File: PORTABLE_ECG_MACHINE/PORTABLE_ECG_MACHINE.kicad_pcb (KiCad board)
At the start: 2 copper layers, 25.5 x 64.8 mm, 71 parts, among them IC1 AD8232ACPZ, J1 UART, J2 Li-Ion 3.7 CONN, J3 USB_B_Micro, Q1 BSS138, Q2 BSS138, SW1 SW_SPDT, U1 SSD1306, U2 CP2102-GM, U3 TC1262-33, U4 TP4056

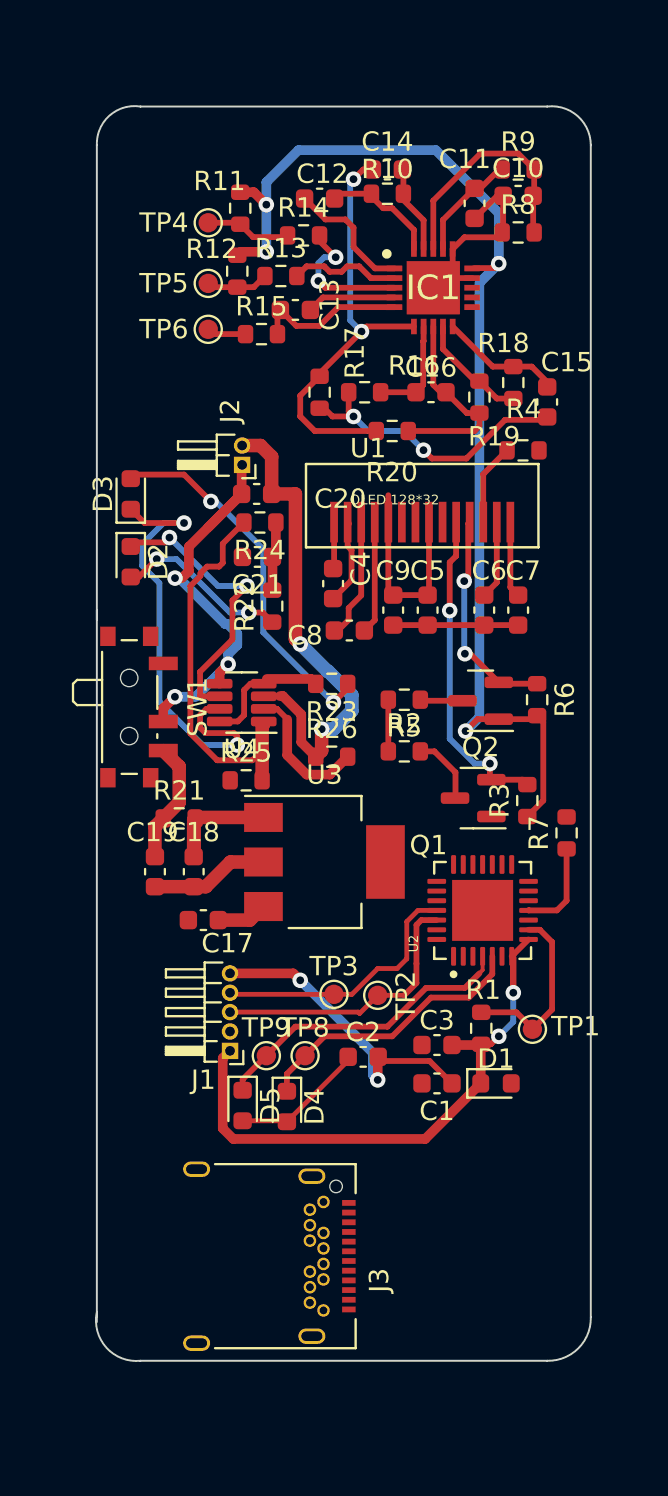
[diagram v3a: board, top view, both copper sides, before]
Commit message: Fill Zone add | Edgecut complete
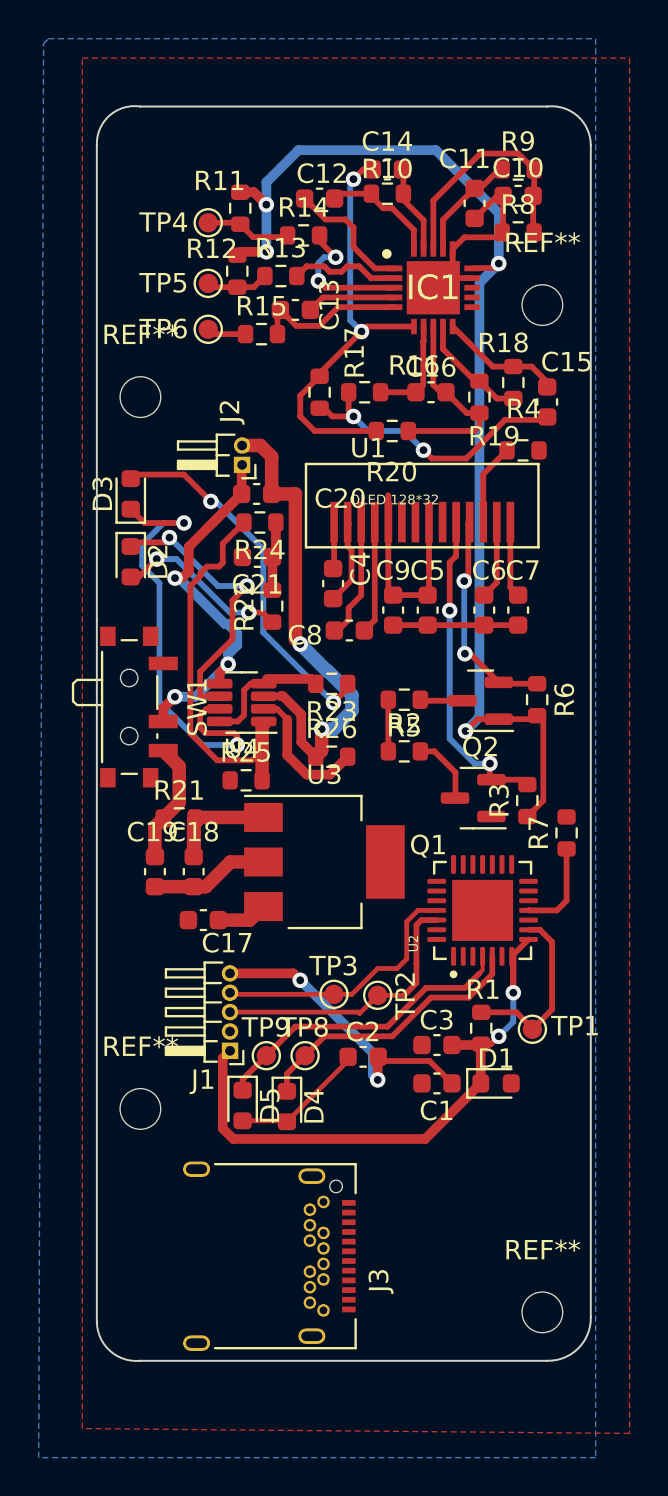
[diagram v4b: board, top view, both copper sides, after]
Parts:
- added REF**: MountingHole_2.1mm, MountingHole:MountingHole_2.1mm, F.Cu at (107.0, 34.8)
- added REF**: MountingHole_2.1mm, MountingHole:MountingHole_2.1mm, F.Cu at (86.2, 76.2)
- added REF**: MountingHole_2.1mm, MountingHole:MountingHole_2.1mm, F.Cu at (86.2, 39.5)
- added REF**: MountingHole_2.1mm, MountingHole:MountingHole_2.1mm, F.Cu at (107.0, 86.8)
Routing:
- added copper zone on B.Cu, net GND
- added copper zone on F.Cu, net GND
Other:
- outline, holes or cut-outs redrawn
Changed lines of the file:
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@@
     )
   )
+  (footprint "MountingHole:MountingHole_2.1mm" (layer "F.Cu")
+    (at 107 34.75)
+    (descr "Mounting Hole 2.1mm, no annular")
+    (tags "mounting hole 2.1mm no annular")
+    (attr exclude_from_pos_files exclude_from_bom)
+    (fp_text reference "REF**" (at 0 -3.2) (layer "F.SilkS")
+      (effects (font (size 1 1) (thickness 0.15)))
+    )
+    (fp_text value "MountingHole_2.1mm" (at 0 3.2) (layer "F.Fab")
+      (effects (font (size 1 1) (thickness 0.15)))
+    )
+    (fp_text user "${REFERENCE}" (at 0 0) (layer "F.Fab")
+      (effects (font (size 1 1) (thickness 0.15)))
+    )
+    (fp_circle (center 0 0) (end 2.1 0) (layer "Cmts.User") (width 0.15) (fill none))
+    (fp_circle (center 0 0) (end 2.35 0) (layer "F.CrtYd") (width 0.05) (fill none))
+    (pad "" np_thru_hole circle (at 0 0) (size 2.1 2.1) (drill 2.1) (layers *.Cu *.Mask))
+  )
   (footprint "Resistor_SMD:R_0603_1608Metric" (layer "F.Cu")
     (at 93.5 33.25)
@@
       (net 25 "/RA") (pinfunction "1") (pintype "passive"))
   )
+  (footprint "MountingHole:MountingHole_2.1mm" (layer "F.Cu")
+    (at 86.25 76.25)
+    (descr "Mounting Hole 2.1mm, no annular")
+    (tags "mounting hole 2.1mm no annular")
+    (attr exclude_from_pos_files exclude_from_bom)
+    (fp_text reference "REF**" (at 0 -3.2) (layer "F.SilkS")
+      (effects (font (size 1 1) (thickness 0.15)))
+    )
+    (fp_text value "MountingHole_2.1mm" (at 0 3.2) (layer "F.Fab")
+      (effects (font (size 1 1) (thickness 0.15)))
+    )
+    (fp_text user "${REFERENCE}" (at 0 0) (layer "F.Fab")
+      (effects (font (size 1 1) (thickness 0.15)))
+    )
+    (fp_circle (center 0 0) (end 2.1 0) (layer "Cmts.User") (width 0.15) (fill none))
+    (fp_circle (center 0 0) (end 2.35 0) (layer "F.CrtYd") (width 0.05) (fill none))
+    (pad "" np_thru_hole circle (at 0 0) (size 2.1 2.1) (drill 2.1) (layers *.Cu *.Mask))
+  )
   (footprint "Capacitor_SMD:C_0603_1608Metric" (layer "F.Cu")
     (at 99 27.75)
@@
     )
   )
+  (footprint "MountingHole:MountingHole_2.1mm" (layer "F.Cu")
+    (at 86.25 39.5)
+    (descr "Mounting Hole 2.1mm, no annular")
+    (tags "mounting hole 2.1mm no annular")
+    (attr exclude_from_pos_files exclude_from_bom)
+    (fp_text reference "REF**" (at 0 -3.2) (layer "F.SilkS")
+      (effects (font (size 1 1) (thickness 0.15)))
+    )
+    (fp_text value "MountingHole_2.1mm" (at 0 3.2) (layer "F.Fab")
+      (effects (font (size 1 1) (thickness 0.15)))
+    )
+    (fp_text user "${REFERENCE}" (at 0 0) (layer "F.Fab")
+      (effects (font (size 1 1) (thickness 0.15)))
+    )
+    (fp_circle (center 0 0) (end 2.1 0) (layer "Cmts.User") (width 0.15) (fill none))
+    (fp_circle (center 0 0) (end 2.35 0) (layer "F.CrtYd") (width 0.05) (fill none))
+    (pad "" np_thru_hole circle (at 0 0) (size 2.1 2.1) (drill 2.1) (layers *.Cu *.Mask))
+  )
   (footprint "Resistor_SMD:R_0603_1608Metric" (layer "F.Cu")
     (at 92.5 36.25)
@@
     )
   )
+  (footprint "MountingHole:MountingHole_2.1mm" (layer "F.Cu")
+    (at 107 86.75)
+    (descr "Mounting Hole 2.1mm, no annular")
+    (tags "mounting hole 2.1mm no annular")
+    (attr exclude_from_pos_files exclude_from_bom)
+    (fp_text reference "REF**" (at 0 -3.2) (layer "F.SilkS")
+      (effects (font (size 1 1) (thickness 0.15)))
+    )
+    (fp_text value "MountingHole_2.1mm" (at 0 3.2) (layer "F.Fab")
+      (effects (font (size 1 1) (thickness 0.15)))
+    )
+    (fp_text user "${REFERENCE}" (at 0 0) (layer "F.Fab")
+      (effects (font (size 1 1) (thickness 0.15)))
+    )
+    (fp_circle (center 0 0) (end 2.1 0) (layer "Cmts.User") (width 0.15) (fill none))
+    (fp_circle (center 0 0) (end 2.35 0) (layer "F.CrtYd") (width 0.05) (fill none))
+    (pad "" np_thru_hole circle (at 0 0) (size 2.1 2.1) (drill 2.1) (layers *.Cu *.Mask))
+  )
   (footprint "Capacitor_SMD:C_0603_1608Metric" (layer "F.Cu")
     (at 92.25 44.5)
@@
     )
   )
-  (gr_line (start 84 50.5) (end 84 87.25) (layer "Edge.Cuts") (width 0.1))
+  (gr_line (start 84 51) (end 84 87.25) (layer "Edge.Cuts") (width 0.1))
   (gr_line (start 86.25 89.25) (end 107.25 89.25) (layer "Edge.Cuts") (width 0.1))
-  (gr_arc (start 84 26.5) (mid 84.652302 24.968215) (end 86.25 24.5) (layer "Edge.Cuts") (width 0.1))
+  (gr_arc (start 84 26.5) (mid 84.652302 24.968214) (end 86.25 24.5) (layer "Edge.Cuts") (width 0.1))
   (gr_line (start 109.5 26.5) (end 109.5 87) (layer "Edge.Cuts") (width 0.1))
-  (gr_arc (start 86.25 89.25) (mid 84.490675 88.570892) (end 84 86.75) (layer "Edge.Cuts") (width 0.1))
+  (gr_arc (start 86.25 89.25) (mid 84.685696 88.744217) (end 84 87.25) (layer "Edge.Cuts") (width 0.1))
   (gr_arc (start 109.5 87) (mid 108.858043 88.608043) (end 107.25 89.25) (layer "Edge.Cuts") (width 0.1))
-  (gr_arc (start 107.25 24.5) (mid 108.82438 24.994447) (end 109.5 26.5) (layer "Edge.Cuts") (width 0.1))
+  (gr_arc (start 107.25 24.5) (mid 108.824385 24.994441) (end 109.5 26.5) (layer "Edge.Cuts") (width 0.1))
   (gr_line (start 86.25 24.5) (end 107.25 24.5) (layer "Edge.Cuts") (width 0.1))
   (gr_line (start 84 51) (end 84 26.5) (layer "Edge.Cuts") (width 0.1))
@@
   (segment (start 93.827765 57.984924) (end 93.827765 56.146035) (width 0.5) (layer "F.Cu") (net 57))
   (segment (start 93.298672 55.5954) (end 93.827765 56.124493) (width 0.3) (layer "F.Cu") (net 57))
+  (zone (net 2) (net_name "GND") (layer "F.Cu") (hatch edge 0.508)
+    (connect_pads (clearance 0.508))
+    (min_thickness 0.254) (filled_areas_thickness no)
+    (fill yes (thermal_gap 0.508) (thermal_bridge_width 0.508))
+    (polygon
+      (pts
+        (xy 111.5 93)
+        (xy 83.25 92.75)
+        (xy 83.25 22)
+        (xy 111.5 22)
+      )
+    )
+  )
+  (zone (net 2) (net_name "GND") (layer "B.Cu") (hatch edge 0.508)
+    (connect_pads (clearance 0.508))
+    (min_thickness 0.254) (filled_areas_thickness no)
+    (fill yes (thermal_gap 0.508) (thermal_bridge_width 0.508))
+    (polygon
+      (pts
+        (xy 109.75 94.25)
+        (xy 81 94.25)
+        (xy 81.25 21.25)
+        (xy 81.5 21)
+        (xy 109.75 21)
+      )
+    )
+  )
 )

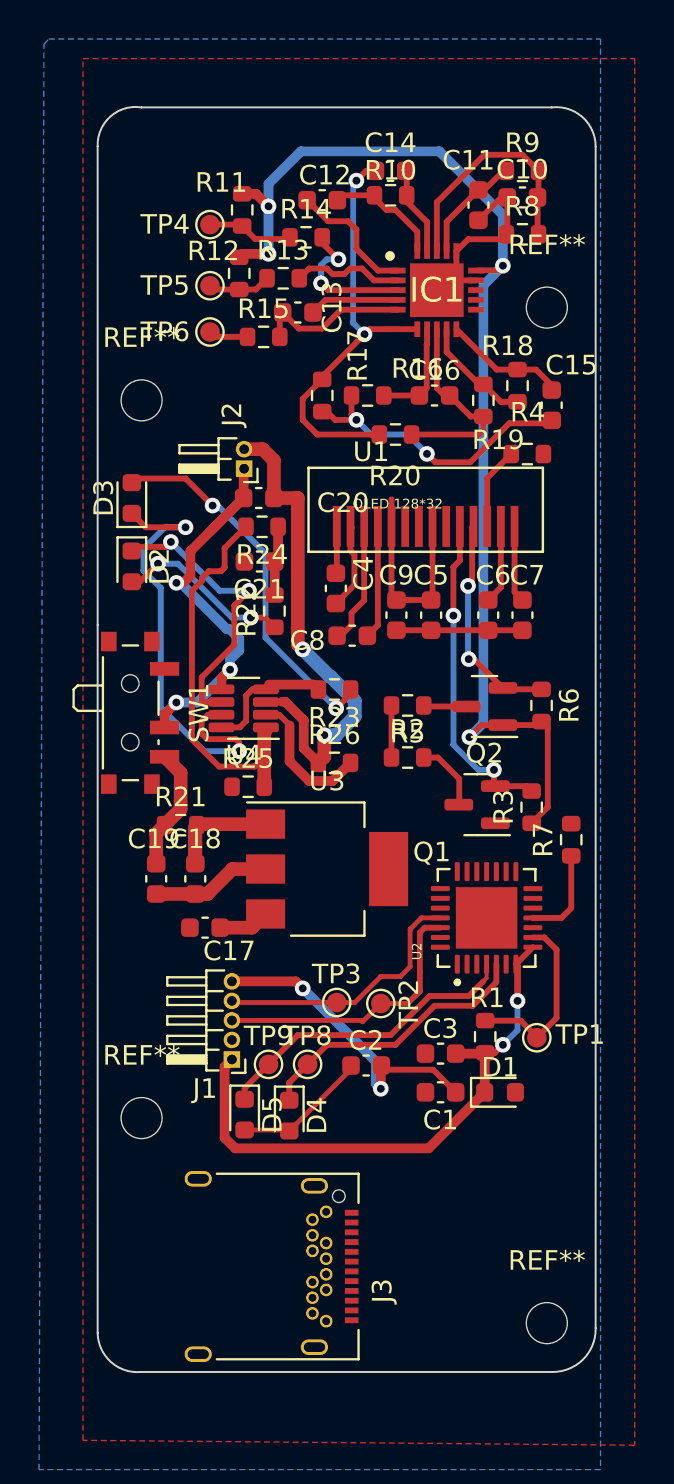
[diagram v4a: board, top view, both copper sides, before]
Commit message: PCBNEW LAYOUT FIX | ADD LIPO-USB_CONN-AUDIO_JACK-TACTILE SWITCH
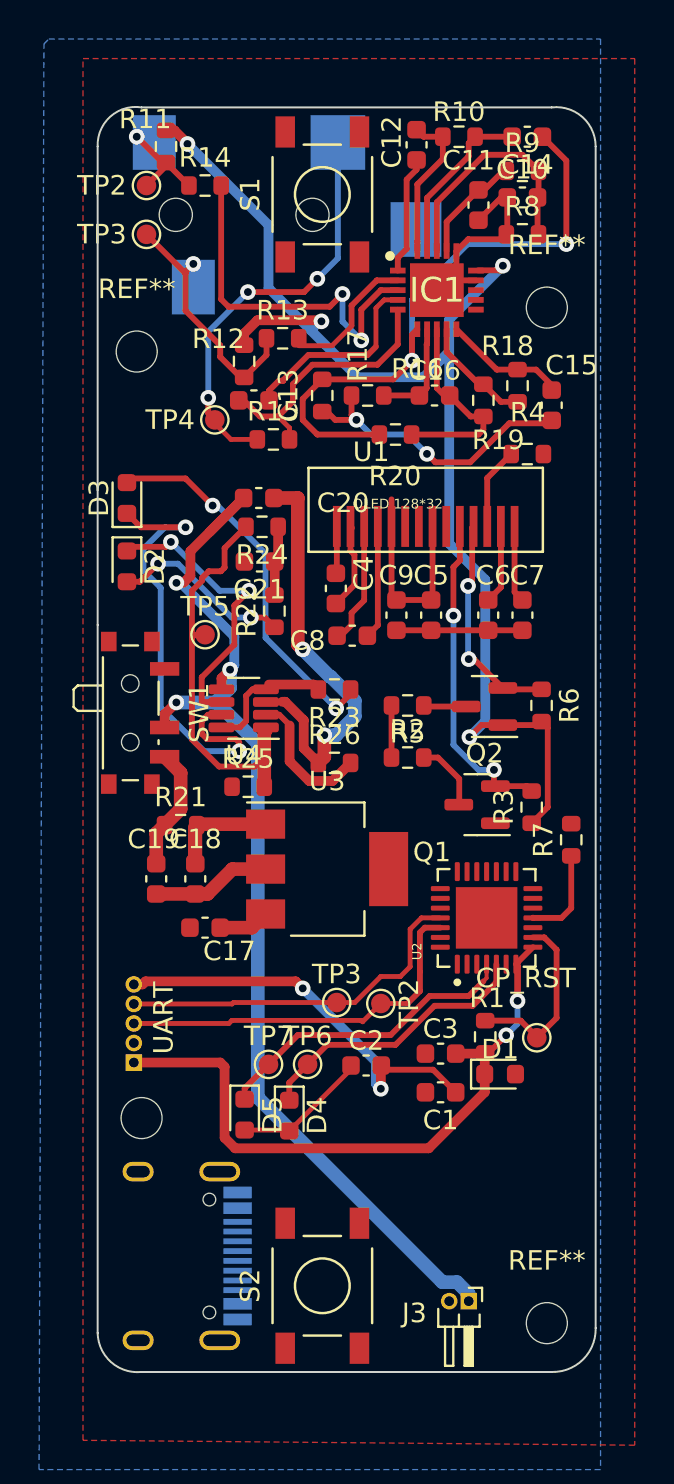
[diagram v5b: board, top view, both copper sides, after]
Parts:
- removed the J3 at (92.0, 83.8)
- added J2: AudioJack3, Connector_Audio:Jack_3.5mm_CUI_SJ-3524-SMT_Horizontal, B.Cu at (90.5, 30.0)
- added J4: USB_C_Receptacle_USB2.0, Connector_USB:USB_C_Receptacle_HRO_TYPE-C-31-M-12, B.Cu at (87.1, 83.3)
- added S1: PTS525SM15SMTR2LFS, tactile switch:SW_PTS525SM15SMTR2LFS, F.Cu at (95.5, 29.0)
- added S2: PTS525SM15SMTR2LFS, tactile switch:SW_PTS525SM15SMTR2LFS, F.Cu at (95.5, 84.8)
- added TP5: B-TEMP, TestPoint:TestPoint_Pad_D1.0mm, F.Cu at (89.5, 51.5)
- J1: moved to B.Cu
- moved J3 44.1 mm to (103.0, 85.6), turned to -90 degrees
- moved C14 7.22 mm to (106.0, 26.0), turned to 180 degrees
- moved R14 5.81 mm to (89.5, 28.5)
- moved C12 5.60 mm to (100.3, 26.4), turned to 90 degrees
- moved R15 5.27 mm to (93.0, 41.5)
- moved R11 5.08 mm to (87.5, 26.5)
- moved C13 5.03 mm to (92.0, 39.5)
- moved J1 5.03 mm to (85.9, 73.4), turned to 0 degrees
- moved R10 4.61 mm to (102.5, 26.0)
- moved R12 4.51 mm to (91.5, 37.5)
- moved TP4 4.51 mm to (90.0, 40.5)
- moved TP3 4.18 mm to (86.5, 31.0)
- moved TP2 3.82 mm to (86.5, 28.5)
- moved R13 3.07 mm to (93.5, 36.3)
- moved REF** 2.51 mm to (86.0, 37.0)
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- renumbered TP1 to CP_RST, J2 to J3, TP4 to TP2, TP5 to TP3, TP6 to TP4, TP8 to TP6, TP9 to TP7, REF** to UART
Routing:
- net /BATTERY +VE: track 22.3 -> 59.5 mm
- net /RL: track 2.03 -> 21.5 mm, vias 0 -> 3
- net Net-(IC1-Pad3): track 7.49 -> 19.1 mm
- net /RA: track 3.24 -> 12.6 mm, vias 0 -> 1
- net Net-(C14-Pad1): track 22.1 -> 31.3 mm
- net 3.3V: track 59.6 -> 65.5 mm
- net Net-(C13-Pad1): track 7.95 -> 13.7 mm
- net Net-(C13-Pad2): track 4.61 -> 10.2 mm
- net Net-(C1-Pad1): track 16.4 -> 21.5 mm
- net /TXD: track 14.5 -> 19.5 mm
- net /RXD: track 13.6 -> 18.6 mm
- net Net-(C14-Pad2): track 4.56 -> 8.77 mm
- net VIN: track 31.2 -> 35.2 mm
- net GND: track 56.8 -> 53.1 mm
- net Net-(C12-Pad2): track 6.04 -> 7.89 mm
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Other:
- board text added: "PORTABLE ECG MACHINE"

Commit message: DRC CHECK
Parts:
- moved R1 2.07 mm to (105.9, 72.1), turned to 0 degrees
- moved CP_RST 1.21 mm to (107.7, 72.1)
- moved TP4 0.91 mm to (89.9, 41.4)
- moved D1 0.87 mm to (105.2, 74.7)
- moved R15 0.66 mm to (93.0, 42.2)
- moved C10 0.63 mm to (105.9, 29.7)
- moved R12 0.59 mm to (90.9, 37.3)
- moved R13 0.57 mm to (93.2, 36.8)
- moved C3 0.55 mm to (102.1, 72.9)
- moved R10 0.51 mm to (102.9, 25.7)
- moved R9 0.47 mm to (105.9, 28.2)
- moved TP2 0.44 mm to (86.1, 28.7)
- moved C14 0.39 mm to (106.2, 25.7)
- moved R16 0.37 mm to (95.5, 39.6)
- moved R11 0.36 mm to (87.4, 26.2)
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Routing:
- net VIN: track 35.2 -> 56.1 mm
- net USB_D-: track 16.0 -> 33.2 mm, vias 0 -> 3
- net USB_D+: track 14.6 -> 29.2 mm, vias 0 -> 1
- net Net-(C1-Pad1): track 21.5 -> 29.6 mm
- net Net-(C21-Pad1): track 10.0 -> 15.2 mm
- net /BATTERY +VE: track 59.5 -> 56.6 mm
- net Net-(D3-Pad1): track 23.7 -> 20.9 mm
- net Net-(R1-Pad2): track 9.34 -> 7.02 mm
- net Net-(C5-Pad2): track 11.0 -> 9.58 mm
- net GND: track 53.1 -> 54.4 mm, vias 2 -> 32
- net Net-(C14-Pad1): track 31.3 -> 32.4 mm
- net /LA: track 5.30 -> 6.08 mm
- net Net-(C12-Pad2): track 7.89 -> 8.62 mm
- net Net-(R24-Pad2): track 20.6 -> 19.9 mm
- net /RL: track 21.5 -> 22.2 mm
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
